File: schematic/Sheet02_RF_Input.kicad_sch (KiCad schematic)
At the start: 4 parts, among them J2 SMA_RF

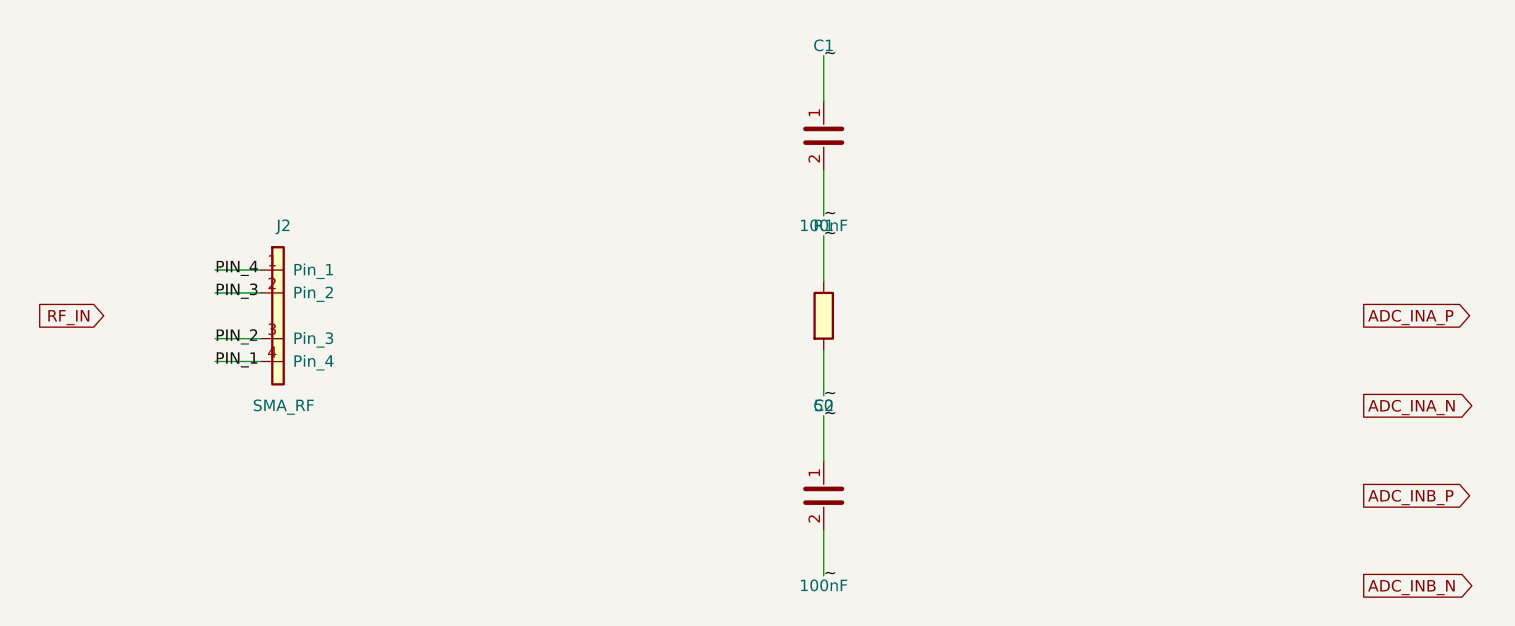
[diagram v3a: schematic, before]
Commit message: Fix KiCad schematic wiring: Y-inversion bug + all 891 pins connected
- Fixed critical Y-axis inversion bug: KiCad inverts Y when placing
  symbols (lib Y + schematic Y = abs Y is WRONG; correct: abs Y = sym Y - lib Y)
- This caused ALL wires to connect to wrong pins (e.g., CS label connected
  to BG pin instead of CS pin)
- Verified with netlist: 0 unconnected nets, all pin functions correct
- Fixed wire direction for angle 90/270 (swapped due to Y-inversion)
- 891 pin connections across 15 sheets, all 17 sheets export without errors
- Netlist verification: CS→E8, BG→C3, INA+→A4, CLK+→F1, JESD pairs correct

Co-Authored-By: opencode <noreply@opencode.ai>
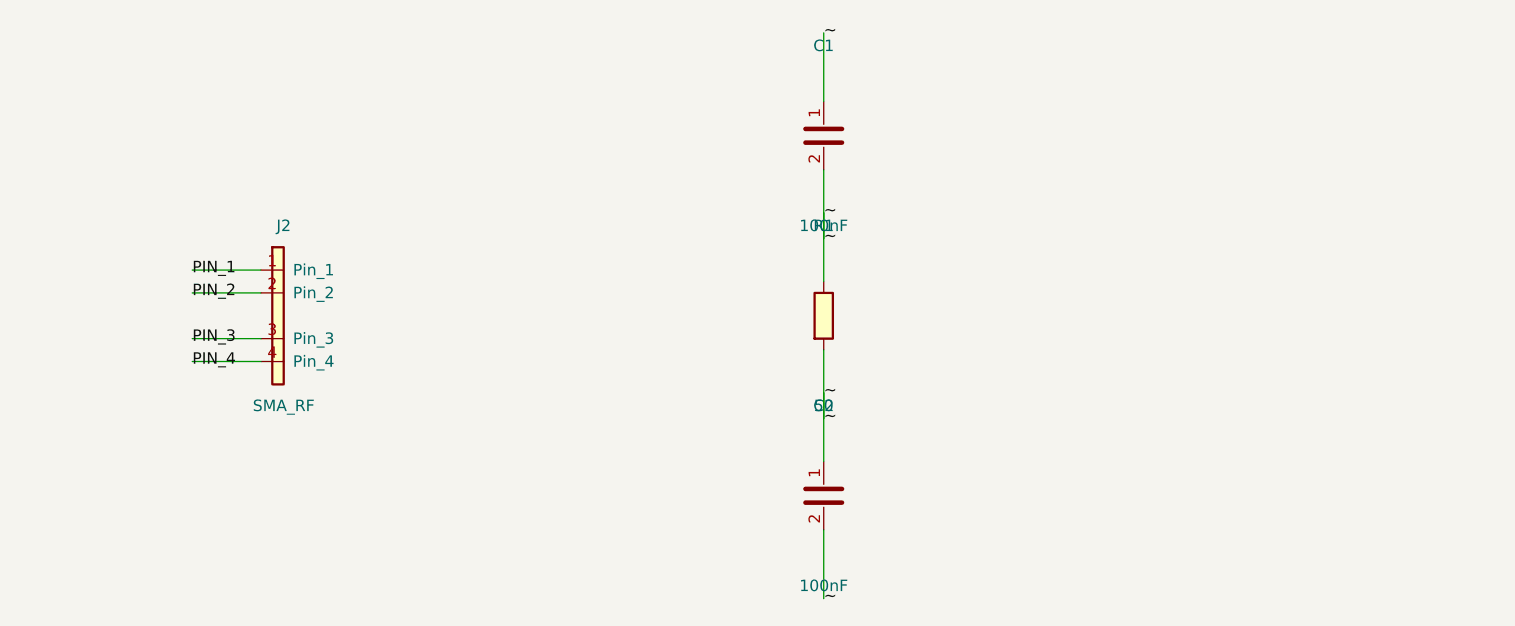
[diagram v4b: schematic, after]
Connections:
- net PIN_1: now also J2.1 (Pin_1); no longer J2.4 (Pin_4)
- net PIN_2: now also J2.2 (Pin_2); no longer J2.3 (Pin_3)
- net PIN_3: now also J2.3 (Pin_3); no longer J2.2 (Pin_2)
- net PIN_4: now also J2.4 (Pin_4); no longer J2.1 (Pin_1)
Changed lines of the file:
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@@
     (pin "1")
     (pin "2")
-  )  (global_label "ADC_INA_P" (shape output) (at 200 60 0) (effects (font (size 1.27 1.27)) (justify left)))  (global_label "ADC_INA_N" (shape output) (at 200 70 0) (effects (font (size 1.27 1.27)) (justify left)))  (global_label "ADC_INB_P" (shape output) (at 200 80 0) (effects (font (size 1.27 1.27)) (justify left)))  (global_label "ADC_INB_N" (shape output) (at 200 90 0) (effects (font (size 1.27 1.27)) (justify left)))  (global_label "RF_IN" (shape input) (at 60 60 180) (effects (font (size 1.27 1.27)) (justify right)))
-  (wire (pts (xy 77.46 65.08) (xy 72.38 65.08)) (stroke (width 0) (type default)))
-  (label "PIN_1" (at 72.38 65.08 0) (effects (font (size 1.27 1.27))))
-  (wire (pts (xy 77.46 62.54) (xy 72.38 62.54)) (stroke (width 0) (type default)))
-  (label "PIN_2" (at 72.38 62.54 0) (effects (font (size 1.27 1.27))))
-  (wire (pts (xy 77.46 57.46) (xy 72.38 57.46)) (stroke (width 0) (type default)))
-  (label "PIN_3" (at 72.38 57.46 0) (effects (font (size 1.27 1.27))))
-  (wire (pts (xy 77.46 54.92) (xy 72.38 54.92)) (stroke (width 0) (type default)))
-  (label "PIN_4" (at 72.38 54.92 0) (effects (font (size 1.27 1.27))))
-  (wire (pts (xy 140.00 63.81) (xy 140.00 68.89)) (stroke (width 0) (type default)))
-  (label "~" (at 140.00 68.89 0) (effects (font (size 1.27 1.27))))
-  (wire (pts (xy 140.00 56.19) (xy 140.00 51.11)) (stroke (width 0) (type default)))
-  (label "~" (at 140.00 51.11 0) (effects (font (size 1.27 1.27))))
-  (wire (pts (xy 140.00 43.81) (xy 140.00 48.89)) (stroke (width 0) (type default)))
-  (label "~" (at 140.00 48.89 0) (effects (font (size 1.27 1.27))))
-  (wire (pts (xy 140.00 36.19) (xy 140.00 31.11)) (stroke (width 0) (type default)))
-  (label "~" (at 140.00 31.11 0) (effects (font (size 1.27 1.27))))
-  (wire (pts (xy 140.00 83.81) (xy 140.00 88.89)) (stroke (width 0) (type default)))
-  (label "~" (at 140.00 88.89 0) (effects (font (size 1.27 1.27))))
-  (wire (pts (xy 140.00 76.19) (xy 140.00 71.11)) (stroke (width 0) (type default)))
-  (label "~" (at 140.00 71.11 0) (effects (font (size 1.27 1.27))))
+  )
+  (wire (pts (xy 77.4600 54.9200) (xy 69.8400 54.9200)) (stroke (width 0) (type default)))
+  (label "PIN_1" (at 69.8400 54.9200 0) (effects (font (size 1.27 1.27))))
+  (wire (pts (xy 77.4600 57.4600) (xy 69.8400 57.4600)) (stroke (width 0) (type default)))
+  (label "PIN_2" (at 69.8400 57.4600 0) (effects (font (size 1.27 1.27))))
+  (wire (pts (xy 77.4600 62.5400) (xy 69.8400 62.5400)) (stroke (width 0) (type default)))
+  (label "PIN_3" (at 69.8400 62.5400 0) (effects (font (size 1.27 1.27))))
+  (wire (pts (xy 77.4600 65.0800) (xy 69.8400 65.0800)) (stroke (width 0) (type default)))
+  (label "PIN_4" (at 69.8400 65.0800 0) (effects (font (size 1.27 1.27))))
+  (wire (pts (xy 140.0000 56.1900) (xy 140.0000 48.5700)) (stroke (width 0) (type default)))
+  (label "~" (at 140.0000 48.5700 0) (effects (font (size 1.27 1.27))))
+  (wire (pts (xy 140.0000 63.8100) (xy 140.0000 71.4300)) (stroke (width 0) (type default)))
+  (label "~" (at 140.0000 71.4300 0) (effects (font (size 1.27 1.27))))
+  (wire (pts (xy 140.0000 36.1900) (xy 140.0000 28.5700)) (stroke (width 0) (type default)))
+  (label "~" (at 140.0000 28.5700 0) (effects (font (size 1.27 1.27))))
+  (wire (pts (xy 140.0000 43.8100) (xy 140.0000 51.4300)) (stroke (width 0) (type default)))
+  (label "~" (at 140.0000 51.4300 0) (effects (font (size 1.27 1.27))))
+  (wire (pts (xy 140.0000 76.1900) (xy 140.0000 68.5700)) (stroke (width 0) (type default)))
+  (label "~" (at 140.0000 68.5700 0) (effects (font (size 1.27 1.27))))
+  (wire (pts (xy 140.0000 83.8100) (xy 140.0000 91.4300)) (stroke (width 0) (type default)))
+  (label "~" (at 140.0000 91.4300 0) (effects (font (size 1.27 1.27))))
   (sheet_instances (path "/" (page "1")))
 )

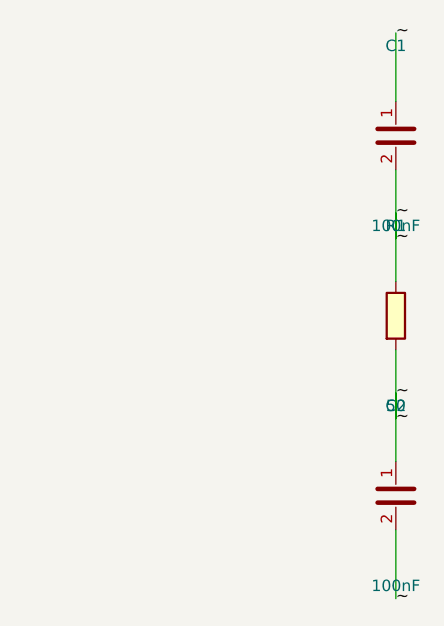
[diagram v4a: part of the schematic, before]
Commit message: fix: use horizontal wire stubs to prevent KiCad net merging
Root cause: vertical wires from stacked power pins (1.27mm spacing)
overlapped when wire length > pin spacing, causing KiCad to merge
all power nets into one. Also skip unnamed (~) passive component pins.

Changes:
- Always use horizontal LEFT stubs regardless of pin angle
- Skip pins with net_name '~' (capacitor/resistor unnamed pins)
- 557 pin connections across 13 sheets, all pass KiCad CLI

NOTE: power net separation still shows all power_in pins on one net
in kicad-cli netlist export - needs further investigation.
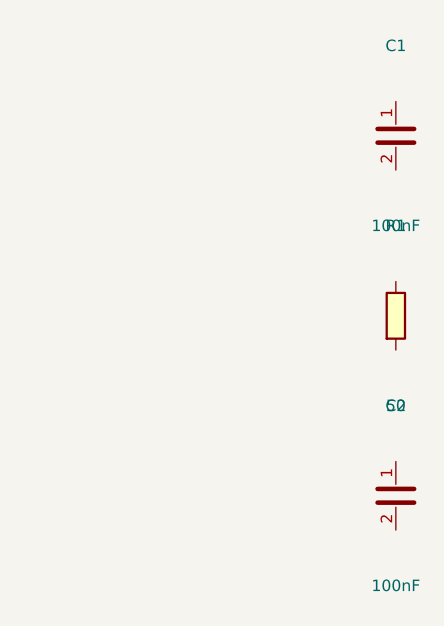
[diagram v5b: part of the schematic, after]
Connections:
- removed net ~: C1.1, C1.2, C2.1, C2.2, R1.1, R1.2
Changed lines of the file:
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@@
   (wire (pts (xy 77.4600 65.0800) (xy 69.8400 65.0800)) (stroke (width 0) (type default)))
   (label "PIN_4" (at 69.8400 65.0800 0) (effects (font (size 1.27 1.27))))
-  (wire (pts (xy 140.0000 56.1900) (xy 140.0000 48.5700)) (stroke (width 0) (type default)))
-  (label "~" (at 140.0000 48.5700 0) (effects (font (size 1.27 1.27))))
-  (wire (pts (xy 140.0000 63.8100) (xy 140.0000 71.4300)) (stroke (width 0) (type default)))
-  (label "~" (at 140.0000 71.4300 0) (effects (font (size 1.27 1.27))))
-  (wire (pts (xy 140.0000 36.1900) (xy 140.0000 28.5700)) (stroke (width 0) (type default)))
-  (label "~" (at 140.0000 28.5700 0) (effects (font (size 1.27 1.27))))
-  (wire (pts (xy 140.0000 43.8100) (xy 140.0000 51.4300)) (stroke (width 0) (type default)))
-  (label "~" (at 140.0000 51.4300 0) (effects (font (size 1.27 1.27))))
-  (wire (pts (xy 140.0000 76.1900) (xy 140.0000 68.5700)) (stroke (width 0) (type default)))
-  (label "~" (at 140.0000 68.5700 0) (effects (font (size 1.27 1.27))))
-  (wire (pts (xy 140.0000 83.8100) (xy 140.0000 91.4300)) (stroke (width 0) (type default)))
-  (label "~" (at 140.0000 91.4300 0) (effects (font (size 1.27 1.27))))
   (sheet_instances (path "/" (page "1")))
 )

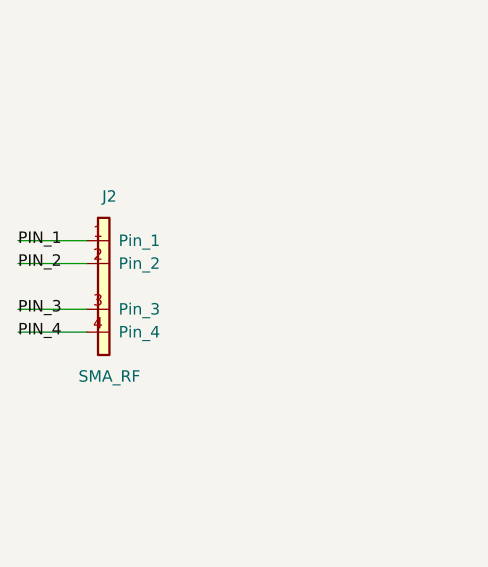
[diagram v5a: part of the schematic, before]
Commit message: fix: replace wire stubs with labels-only to prevent power net shorts
Labels placed directly at pin endpoints eliminate wire overlap that
caused BGA power pins (VA11, VA19, VD11, AGND, DGND) to merge into
a single net. Verified via netlist: GND=52, +1V0_ANA=12, +1V9_ANA=12,
+1V1_DIG=10 nodes (all correct per datasheet pin mapping).
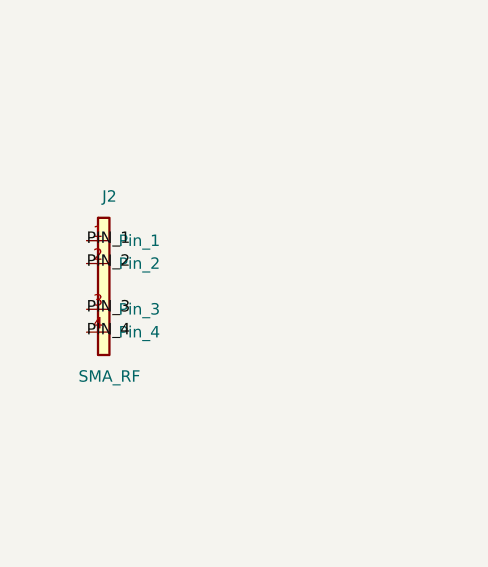
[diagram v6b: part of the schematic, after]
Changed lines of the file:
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@@
     (pin "2")
   )
-  (wire (pts (xy 77.4600 54.9200) (xy 69.8400 54.9200)) (stroke (width 0) (type default)))
-  (label "PIN_1" (at 69.8400 54.9200 0) (effects (font (size 1.27 1.27))))
-  (wire (pts (xy 77.4600 57.4600) (xy 69.8400 57.4600)) (stroke (width 0) (type default)))
-  (label "PIN_2" (at 69.8400 57.4600 0) (effects (font (size 1.27 1.27))))
-  (wire (pts (xy 77.4600 62.5400) (xy 69.8400 62.5400)) (stroke (width 0) (type default)))
-  (label "PIN_3" (at 69.8400 62.5400 0) (effects (font (size 1.27 1.27))))
-  (wire (pts (xy 77.4600 65.0800) (xy 69.8400 65.0800)) (stroke (width 0) (type default)))
-  (label "PIN_4" (at 69.8400 65.0800 0) (effects (font (size 1.27 1.27))))
+  (label "PIN_1" (at 77.4600 54.9200 0) (effects (font (size 1.27 1.27))))
+  (label "PIN_2" (at 77.4600 57.4600 0) (effects (font (size 1.27 1.27))))
+  (label "PIN_3" (at 77.4600 62.5400 0) (effects (font (size 1.27 1.27))))
+  (label "PIN_4" (at 77.4600 65.0800 0) (effects (font (size 1.27 1.27))))
   (sheet_instances (path "/" (page "1")))
 )

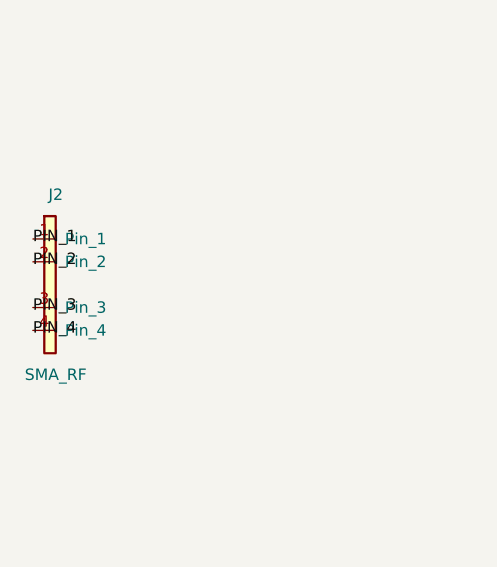
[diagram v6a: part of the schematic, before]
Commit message: fix: isolate ISL70003ASEH buck pins, fix LMX_SYNC collision, NC pins, connector pin names
- ISL70003ASEH pins now use ref prefix (U6_LX1 vs U7_LX1) to prevent shorts
- Buck SYNC pins separated from LMX_SYNC (power sync ≠ PLL sync)
- NC pins properly skipped (unconnected)
- Connector PIN_1..PIN_6 use ref prefix (J1_PIN_1 vs J2_PIN_1)
- Fixed annotation warnings in Sheet13 (C_dev→C125, R_dev→R74, U_TPS7H→U14)
- Regenerated all PDFs and SVGs
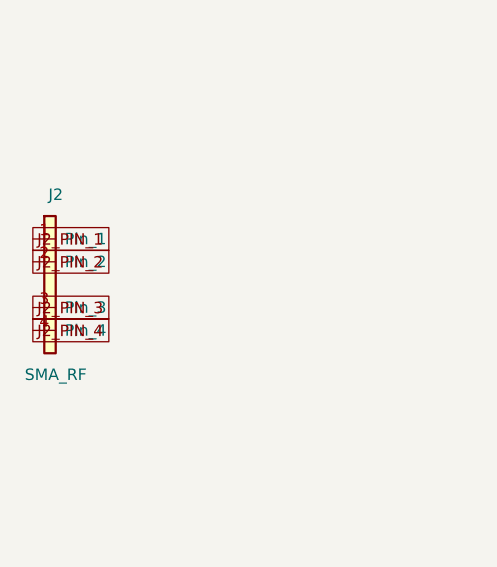
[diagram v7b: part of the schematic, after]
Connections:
- net PIN_1 renamed J2_PIN_1
- net PIN_2 renamed J2_PIN_2
- net PIN_3 renamed J2_PIN_3
- net PIN_4 renamed J2_PIN_4
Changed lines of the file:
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@@
     (pin "2")
   )
-  (label "PIN_1" (at 77.4600 54.9200 0) (effects (font (size 1.27 1.27))))
-  (label "PIN_2" (at 77.4600 57.4600 0) (effects (font (size 1.27 1.27))))
-  (label "PIN_3" (at 77.4600 62.5400 0) (effects (font (size 1.27 1.27))))
-  (label "PIN_4" (at 77.4600 65.0800 0) (effects (font (size 1.27 1.27))))
+  (global_label "J2_PIN_1" (at 77.4600 54.9200 0) (effects (font (size 1.27 1.27))))
+  (global_label "J2_PIN_2" (at 77.4600 57.4600 0) (effects (font (size 1.27 1.27))))
+  (global_label "J2_PIN_3" (at 77.4600 62.5400 0) (effects (font (size 1.27 1.27))))
+  (global_label "J2_PIN_4" (at 77.4600 65.0800 0) (effects (font (size 1.27 1.27))))
   (sheet_instances (path "/" (page "1")))
 )

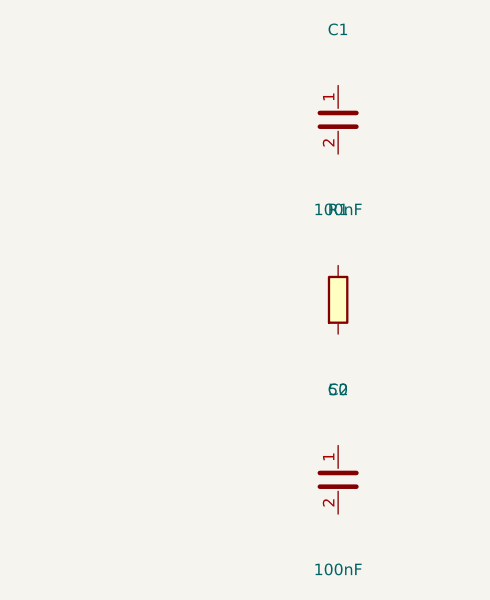
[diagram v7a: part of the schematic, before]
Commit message: feat: connect ALL passive components and fix clock routing
- Added PASSIVE_TOPOLOGY dict mapping 139 passives to their nets
- Passive pin endpoints now get global_labels (was 0 connected, now 138)
- R38 intentionally GND-GND (RECAL_EN pull-down)
- Fixed LMK clock output mapping: CLKout0→ADC_CLK_P, CLKout2→FPGA_REFCLK_P, etc.
- Fixed TPS7H5001-SP SYNC pin collision with LMX_SYNC
- Total connections: 867 pins (up from 641)
- Cross-sheet nets: 52
- Power rails: VIN(33), +3V3(98), GND(228) all with decoupling
- JESD204C: U1↔U2 on 4 lanes ✓
- SPI: U1↔U2↔U3↔U4 ✓
- Clock: LMK→ADC (CLK+SYSREF), LMK→FPGA (REF+SPW) ✓
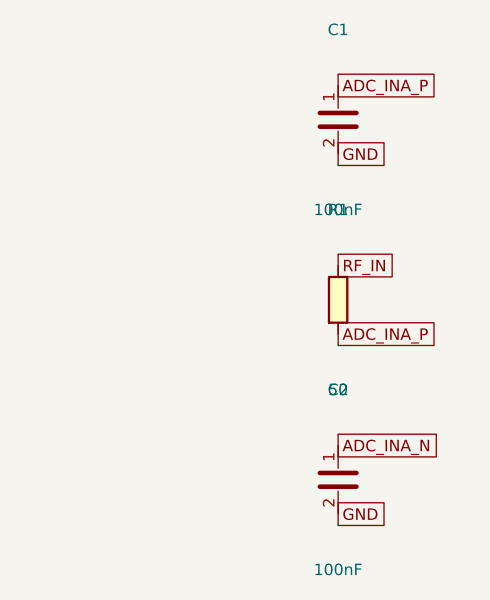
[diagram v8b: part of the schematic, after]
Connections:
- net ADC_INA_N: now reaches C2.1
- net GND: now reaches C2.2
- net GND: now also C1.2
- net RF_IN: now reaches R1.1
- net ADC_INA_P: now reaches R1.2
- net ADC_INA_P: now also C1.1
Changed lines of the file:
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@@
   (global_label "J2_PIN_3" (at 77.4600 62.5400 0) (effects (font (size 1.27 1.27))))
   (global_label "J2_PIN_4" (at 77.4600 65.0800 0) (effects (font (size 1.27 1.27))))
+  (global_label "RF_IN" (at 140.0000 56.1900 0) (effects (font (size 1.27 1.27))))
+  (global_label "ADC_INA_P" (at 140.0000 63.8100 0) (effects (font (size 1.27 1.27))))
+  (global_label "ADC_INA_P" (at 140.0000 36.1900 0) (effects (font (size 1.27 1.27))))
+  (global_label "GND" (at 140.0000 43.8100 0) (effects (font (size 1.27 1.27))))
+  (global_label "ADC_INA_N" (at 140.0000 76.1900 0) (effects (font (size 1.27 1.27))))
+  (global_label "GND" (at 140.0000 83.8100 0) (effects (font (size 1.27 1.27))))
   (sheet_instances (path "/" (page "1")))
 )
